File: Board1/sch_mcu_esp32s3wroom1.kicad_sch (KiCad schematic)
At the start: 11 parts, among them J7 ESPFlash, SW1 Boot, SW2 Reset, U1 ESP32-S3-WROOM-1

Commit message: Resolve library and ERC issues
No changes to design.
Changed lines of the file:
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@@
 		)
 	)
-	(text_box "DESIGN NOTE:\n\nThis could be removed in favour of a USB connectorhowever cost uplift and slightly more complex to route. The firmware is unlikely to be updated often AND could be done OTA."
+	(text_box "DESIGN NOTE:\n\nThis could be removed in favour of a USB connector however cost uplift and slightly more complex to route. The firmware is unlikely to be updated often and after initial flash, could be done OTA."
 		(exclude_from_sim no)
 		(at 187.96 83.185 0)
@@
 			)
 		)
-		(property "Datasheet" "http://www.apem.com/int/index.php?controller=attachment&id_attachment=1371"
+		(property "Datasheet" "https://www.ckswitches.com/media/1476/pts810.pdf"
 			(at 161.29 50.8 0)
 			(effects
@@
 			)
 		)
-		(property "Datasheet" "http://www.apem.com/int/index.php?controller=attachment&id_attachment=1371"
+		(property "Datasheet" "https://www.ckswitches.com/media/1476/pts810.pdf"
 			(at 207.01 48.26 0)
 			(effects

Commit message: v1.2 release of board with bug fixes etc
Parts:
- C6: value 10u -> 22u; Digikey_PN 490-6473-1-ND -> 1276-2909-1-ND; Supplier https://www.digikey.co.nz/en/products/detail/murata-electro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 -> https://www.digikey.co.nz/en/products/detail/samsung-electr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
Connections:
- net ROTARY_BTN: now also U1.23 (IO21); no longer U1.25 (IO48)
- net ROTARY_SIG: now also U1.25 (IO48); no longer U1.23 (IO21)
- net THERMO_CS: no longer names the net of U1.21 (IO13)
- net THERMO_MISO: no longer names the net of U1.20 (IO12)
- net THERMO_SCK: no longer names the net of U1.22 (IO14)
- no-connect marks 20 -> 23
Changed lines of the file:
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@@
 (kicad_sch
-	(version 20231120)
+	(version 20250114)
 	(generator "eeschema")
-	(generator_version "8.0")
+	(generator_version "9.0")
 	(paper "A4")
 	(title_block
 		(title "ESP32-S3-WROOM-1 Module")
-		(date "2025-02-19")
-		(rev "1.1")
+		(date "2025-03-08")
+		(rev "1.2")
 		(company "Wattle Labs")
+	)
+	(text "I2C Pullups"
+		(exclude_from_sim no)
+		(at 246.888 40.386 0)
+		(effects
+			(font
+				(size 1.27 1.27)
+			)
+		)
+	)
+	(text "ESP32 Reset"
+		(exclude_from_sim no)
+		(at 160.782 40.386 0)
+		(effects
+			(font
+				(size 1.27 1.27)
+			)
+		)
+	)
+	(text "ESP32 Boot"
+		(exclude_from_sim no)
+		(at 205.994 40.386 0)
+		(effects
+			(font
+				(size 1.27 1.27)
+			)
+		)
+	)
+	(text "ESPFlash Connector"
+		(exclude_from_sim no)
+		(at 164.592 84.836 0)
+		(effects
+			(font
+				(size 1.27 1.27)
+			)
+		)
+	)
+	(text_box "DESIGN NOTE:\n\nThis could be removed in favour of a USB connector however cost uplift and slightly more complex to route. The firmware is unlikely to be updated often and after initial flash, could be done OTA."
+		(exclude_from_sim no)
+		(at 187.96 83.185 0)
+		(size 59.055 14.605)
+		(margins 1.2025 1.2025 1.2025 1.2025)
+		(stroke
+			(width 0.5)
+			(type solid)
+			(color 200 200 200 1)
+		)
+		(fill
+			(type none)
+		)
+		(effects
+			(font
+				(size 1.27 1.27)
+				(color 0 0 0 1)
+			)
+			(justify left top)
+		)
+	)
+	(text_box "[${#}] ${TITLE}"
+		(exclude_from_sim no)
+		(at 12.065 12.065 0)
+		(size 273.05 13.335)
+		(margins 2.2499 2.2499 2.2499 2.2499)
+		(stroke
+			(width -0.0001)
+			(type default)
+		)
+		(fill
+			(type none)
+		)
+		(effects
+			(font
+				(size 3 3)
+				(thickness 0.375)
+			)
+		)
 	)
 	(junction
@@
 	)
 	(no_connect
+		(at 44.45 100.33)
+	)
+	(no_connect
 		(at 48.26 69.85)
 	)
 	(no_connect
+		(at 44.45 95.25)
+	)
+	(no_connect
 		(at 78.74 82.55)
 	)
@@
 	)
 	(no_connect
+		(at 44.45 97.79)
+	)
+	(no_connect
 		(at 48.26 74.93)
 	)
@@
 	(wire
 		(pts
+			(xy 78.74 105.41) (xy 82.55 105.41)
+		)
+		(stroke
+			(width 0)
+			(type default)
+		)
+	)
+	(wire
+		(pts
 			(xy 261.62 48.26) (xy 261.62 57.15)
 		)
@@
 	(wire
 		(pts
+			(xy 82.55 74.93) (xy 78.74 74.93)
+		)
+		(stroke
+			(width 0)
+			(type default)
+		)
+	)
+	(wire
+		(pts
 			(xy 154.94 55.88) (xy 154.94 63.5)
 		)
@@
 	(wire
 		(pts
-			(xy 78.74 74.93) (xy 83.82 74.93)
-		)
-		(stroke
-			(width 0)
-			(type default)
-		)
-	)
-	(wire
-		(pts
 			(xy 78.74 67.31) (xy 82.55 67.31)
 		)
@@
 	(wire
 		(pts
-			(xy 78.74 105.41) (xy 82.55 105.41)
-		)
-		(stroke
-			(width 0)
-			(type default)
-		)
-	)
-	(wire
-		(pts
 			(xy 99.06 45.72) (xy 111.76 45.72)
 		)
@@
 			(width 0)
 			(type default)
-		)
-	)
-	(text_box "DESIGN NOTE:\n\nThis could be removed in favour of a USB connector however cost uplift and slightly more complex to route. The firmware is unlikely to be updated often and after initial flash, could be done OTA."
-		(exclude_from_sim no)
-		(at 187.96 83.185 0)
-		(size 59.055 14.605)
-		(stroke
-			(width 0.5)
-			(type solid)
-			(color 200 200 200 1)
-		)
-		(fill
-			(type none)
-		)
-		(effects
-			(font
-				(size 1.27 1.27)
-				(color 0 0 0 1)
-			)
-			(justify left top)
-		)
-	)
-	(text_box "[${#}] ${TITLE}"
-		(exclude_from_sim no)
-		(at 12.065 12.065 0)
-		(size 273.05 13.335)
-		(stroke
-			(width -0.0001)
-			(type default)
-		)
-		(fill
-			(type none)
-		)
-		(effects
-			(font
-				(size 3 3)
-				(thickness 0.375)
-			)
-		)
-	)
-	(text "I2C Pullups"
-		(exclude_from_sim no)
-		(at 246.888 40.386 0)
-		(effects
-			(font
-				(size 1.27 1.27)
-			)
-		)
-	)
-	(text "ESP32 Reset"
-		(exclude_from_sim no)
-		(at 160.782 40.386 0)
-		(effects
-			(font
-				(size 1.27 1.27)
-			)
-		)
-	)
-	(text "ESP32 Boot"
-		(exclude_from_sim no)
-		(at 205.994 40.386 0)
-		(effects
-			(font
-				(size 1.27 1.27)
-			)
-		)
-	)
-	(text "ESPFlash Connector"
-		(exclude_from_sim no)
-		(at 164.592 84.836 0)
-		(effects
-			(font
-				(size 1.27 1.27)
-			)
 		)
 	)
@@
 		)
 	)
-	(global_label "THERMO_SCK"
-		(shape input)
-		(at 44.45 100.33 180)
-		(fields_autoplaced yes)
-		(effects
-			(font
-				(size 1.27 1.27)
-			)
-			(justify right)
-		)
-		(property "Intersheetrefs" "${INTERSHEET_REFS}"
-			(at 29.9029 100.33 0)
-			(effects
-				(font
-					(size 1.27 1.27)
-				)
-				(justify right)
-				(hide yes)
-			)
-		)
-	)
 	(global_label "ROTARY_BTN"
 		(shape input)
-		(at 82.55 105.41 0)
+		(at 82.55 74.93 0)
 		(fields_autoplaced yes)
 		(effects
@@
 		)
 		(property "Intersheetrefs" "${INTERSHEET_REFS}"
-			(at 96.432 105.41 0)
+			(at 96.432 74.93 0)
 			(effects
 				(font
@@
 				)
 				(justify left)
-				(hide yes)
-			)
-		)
-	)
-	(global_label "THERMO_MISO"
-		(shape input)
-		(at 44.45 95.25 180)
-		(fields_autoplaced yes)
-		(effects
-			(font
-				(size 1.27 1.27)
-			)
-			(justify right)
-		)
-		(property "Intersheetrefs" "${INTERSHEET_REFS}"
-			(at 29.0562 95.25 0)
-			(effects
-				(font
-					(size 1.27 1.27)
-				)
-				(justify right)
 				(hide yes)
 			)
@@
 		)
 	)
-	(global_label "THERMO_CS"
-		(shape input)
-		(at 44.45 97.79 180)
-		(fields_autoplaced yes)
-		(effects
-			(font
-				(size 1.27 1.27)
-			)
-			(justify right)
-		)
-		(property "Intersheetrefs" "${INTERSHEET_REFS}"
-			(at 31.1729 97.79 0)
-			(effects
-				(font
-					(size 1.27 1.27)
-				)
-				(justify right)
-				(hide yes)
-			)
-		)
-	)
 	(global_label "ESP_TXD"
 		(shape input)
@@
 	(global_label "ROTARY_SIG"
 		(shape input)
-		(at 83.82 74.93 0)
+		(at 82.55 105.41 0)
 		(fields_autoplaced yes)
 		(effects
@@
 		)
 		(property "Intersheetrefs" "${INTERSHEET_REFS}"
-			(at 97.2182 74.93 0)
+			(at 95.9482 105.41 0)
 			(effects
 				(font
@@
 			)
 		)
-		(property "Value" "10u"
+		(property "Value" "22u"
 			(at 114.3 50.8062 0)
 			(effects
@@
 			)
 		)
-		(property "Description" "10 µF ±10% 16V Ceramic Capacitor X5R 0805 (2012 Metric)"
+		(property "Description" "22 µF ±20% 16V Ceramic Capacitor X5R 0805 (2012 Metric)"
 			(at 111.76 49.53 0)
 			(effects
@@
 			)
 		)
-		(property "Supplier" "https://www.digikey.co.nz/en/products/detail/murata-electronics/GRM21BR61C106KE15K/2546903"
+		(property "Supplier" "https://www.digikey.co.nz/en/products/detail/samsung-electro-mechanics/CL21A226MOQNNNE/3888567"
 			(at 111.76 49.53 0)
 			(effects
@@
 			)
 		)
-		(property "Digikey_PN" "490-6473-1-ND"
+		(property "Digikey_PN" "1276-2909-1-ND"
 			(at 111.76 49.53 0)
 			(effects

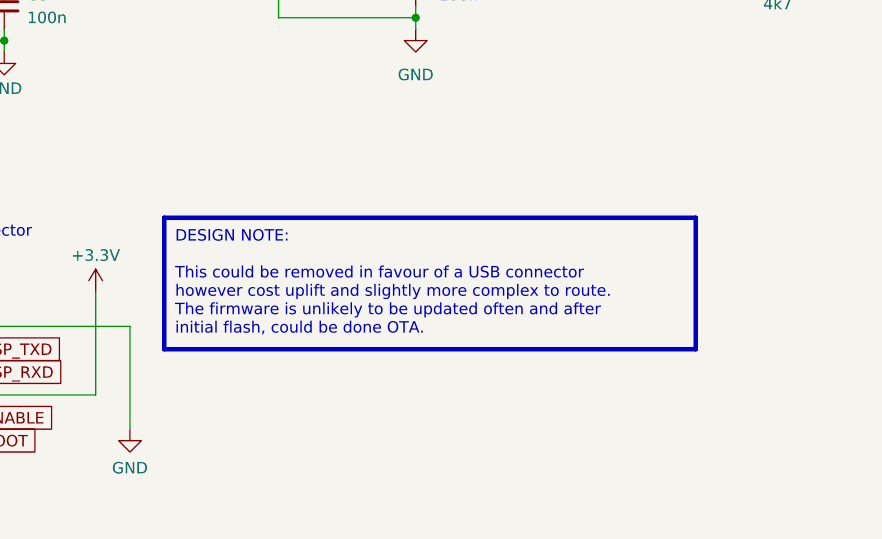
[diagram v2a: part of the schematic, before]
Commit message: Tweaks to schematic for clarity and minor firmware
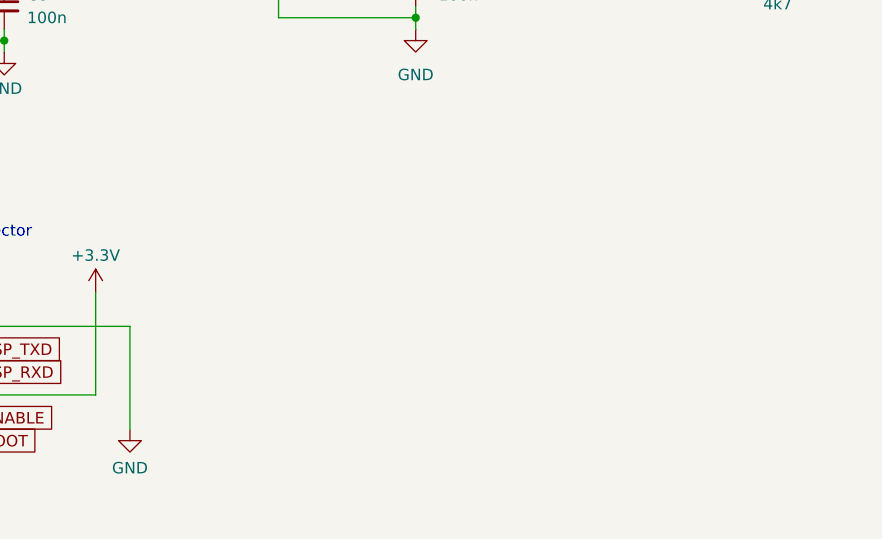
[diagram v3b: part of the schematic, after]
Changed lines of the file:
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@@
 	(title_block
 		(title "ESP32-S3-WROOM-1 Module")
-		(date "2025-03-08")
+		(date "2025-03-10")
 		(rev "1.2")
 		(company "Wattle Labs")
@@
 		)
 	)
-	(text_box "DESIGN NOTE:\n\nThis could be removed in favour of a USB connector however cost uplift and slightly more complex to route. The firmware is unlikely to be updated often and after initial flash, could be done OTA."
-		(exclude_from_sim no)
-		(at 187.96 83.185 0)
-		(size 59.055 14.605)
-		(margins 1.2025 1.2025 1.2025 1.2025)
-		(stroke
-			(width 0.5)
-			(type solid)
-			(color 200 200 200 1)
-		)
-		(fill
-			(type none)
-		)
-		(effects
-			(font
-				(size 1.27 1.27)
-				(color 0 0 0 1)
-			)
-			(justify left top)
-		)
-	)
